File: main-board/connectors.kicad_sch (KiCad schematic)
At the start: 26 parts, among them J1 USB_C_Receptacle_USB2.0_16P, J2 USB_C_Receptacle_PowerOnly_6P, J3 Conn_01x02, J4 Conn_ARM_SWD_TagConnect_TC203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, U24 TMUX154ERSW, U5 FUSB302B10MPX, U6 FUSB302B11MPX, U9 FUSB302B01MPX

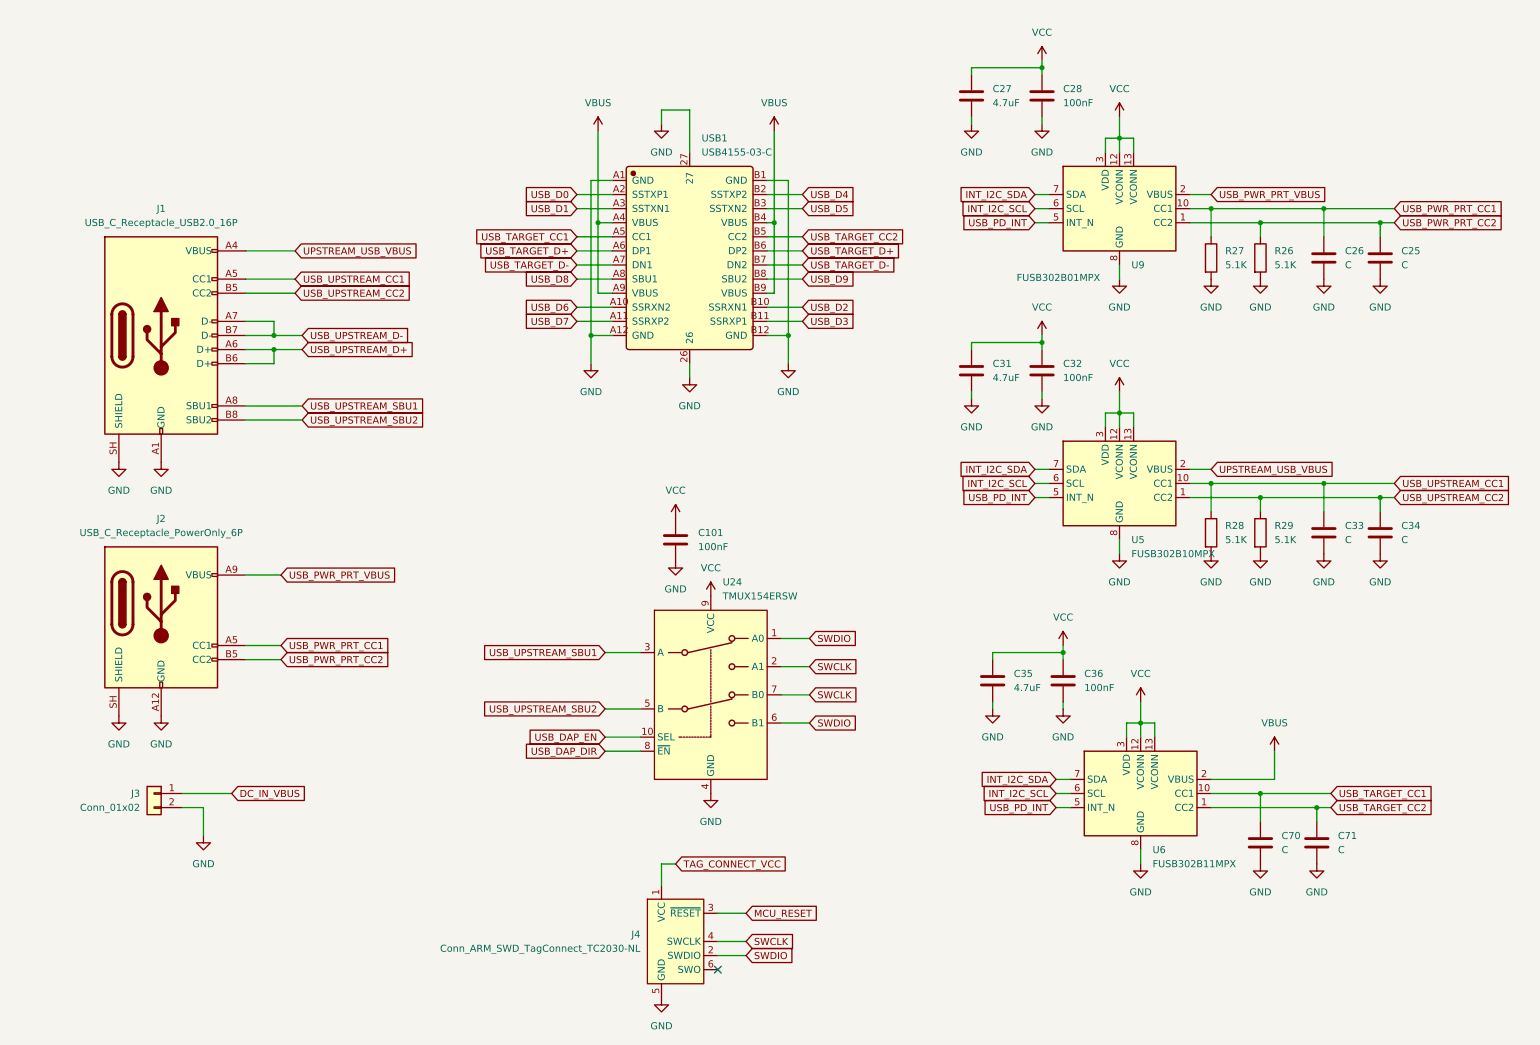
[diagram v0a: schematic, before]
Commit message: Divide pcb into 2 and start routing
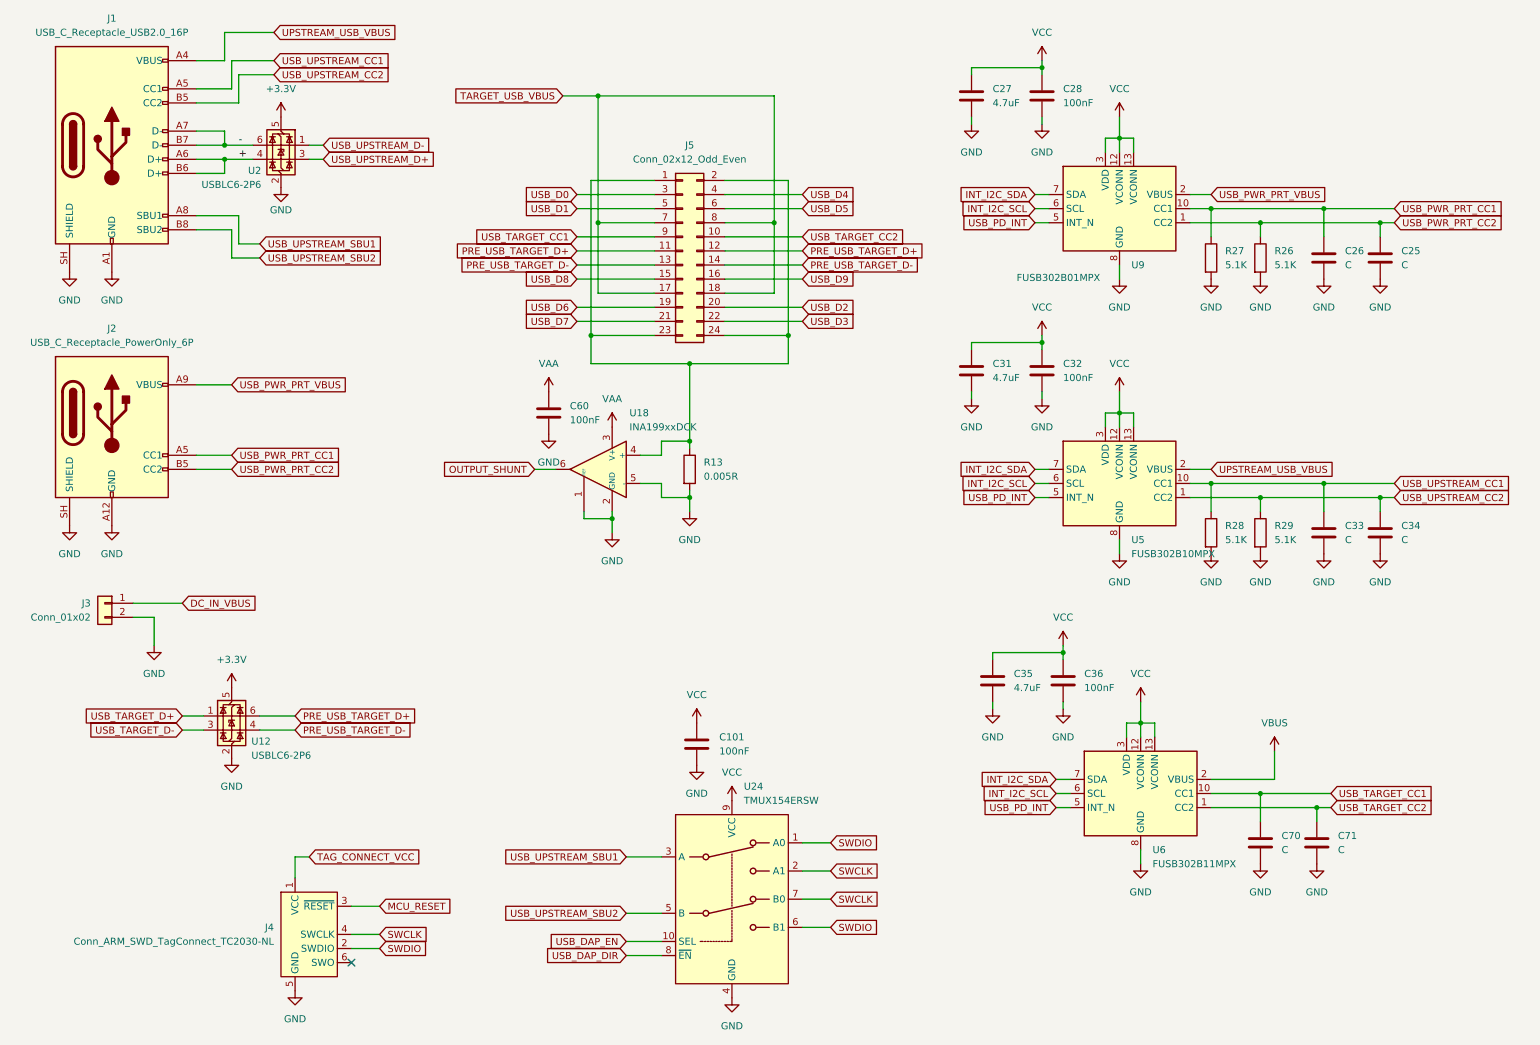
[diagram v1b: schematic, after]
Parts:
- removed USB1: USB4155-03-C, JLCImport:USB4155-03-C, symbol JLCImport:USB4155-03-C
- added C60: 100nF, Capacitor_SMD:C_0805_2012Metric, symbol Device:C
- added J5: Conn_02x12_Odd_Even, Connector_PinSocket_2.54mm:PinSocket_2x12_P2.54mm_Horizontal, symbol Connector_Generic:Conn_02x12_Odd_Even
- added R13: 0.005R, Resistor_SMD:R_1206_3216Metric, symbol Device:R
- added U12, U2: USBLC6-2P6, Package_TO_SOT_SMD:SOT-666, symbol Power_Protection:USBLC6-2P6
- added U18: INA199xxDCK, Package_TO_SOT_SMD:SOT-363_SC-70-6, symbol Amplifier_Current:INA199xxDCK
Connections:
- net GND: now also C60.2, R13.2, U12.2 (GND), U18.1 (REF), U18.2 (GND), U18.5 (-), U2.2 (GND)
- net USB_D0: now also J5.3 (Pin_3)
- net USB_D1: now also J5.5 (Pin_5)
- net USB_D2: now also J5.20 (Pin_20)
- net USB_D3: now also J5.22 (Pin_22)
- net USB_D4: now also J5.4 (Pin_4)
- net USB_D5: now also J5.6 (Pin_6)
- net USB_D6: now also J5.19 (Pin_19)
- net USB_D7: now also J5.21 (Pin_21)
- net USB_D8: now also J5.15 (Pin_15)
- net USB_D9: now also J5.16 (Pin_16)
- net USB_TARGET_CC1: now also J5.9 (Pin_9)
- net USB_TARGET_CC2: now also J5.10 (Pin_10)
- net USB_TARGET_D+: now also U12.1 (I/O1)
- net USB_TARGET_D-: now also U12.3 (I/O2)
- net USB_UPSTREAM_D+: now also U2.3 (I/O2); no longer J1.A6 (D+), J1.B6 (D+)
- net USB_UPSTREAM_D-: now also U2.1 (I/O1); no longer J1.A7 (D-), J1.B7 (D-)
- new net: J5.1 (Pin_1), J5.2 (Pin_2), J5.23 (Pin_23), J5.24 (Pin_24), R13.1, U18.4 (+)
- new net +: J1.A6 (D+), J1.B6 (D+), U2.4 (I/O2)
- new net +3.3V: U12.5 (VBUS), U2.5 (VBUS)
- new net -: J1.A7 (D-), J1.B7 (D-), U2.6 (I/O1)
- new net OUTPUT_SHUNT: U18.6
- new net PRE_USB_TARGET_D+: J5.11 (Pin_11), J5.12 (Pin_12), U12.6 (I/O1)
- new net PRE_USB_TARGET_D-: J5.13 (Pin_13), J5.14 (Pin_14), U12.4 (I/O2)
- new net TARGET_USB_VBUS: J5.17 (Pin_17), J5.18 (Pin_18), J5.7 (Pin_7), J5.8 (Pin_8)
- new net VAA: C60.1, U18.3 (V+)
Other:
- moved on the sheet: C101, J1, J2, J3, J4, U24

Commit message: Finish routing
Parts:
- C101: footprint Capacitor_SMD:C_0402_1005Metric -> Capacitor_SMD:C_0805_2012Metric
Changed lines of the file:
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@@
 			)
 		)
-		(property "Footprint" "Capacitor_SMD:C_0402_1005Metric"
+		(property "Footprint" "Capacitor_SMD:C_0805_2012Metric"
 			(at 133.0452 146.05 0)
 			(hide yes)
